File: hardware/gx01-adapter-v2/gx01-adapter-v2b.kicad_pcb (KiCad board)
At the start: 2 copper layers, 65 x 56.5 mm, 26 parts, among them J1 Pi GPIO 40-pin, J2 LCD 2x10 IDC, J3 Fan 1, J4 Fan 2, J5 FPB cable, Q1 AO3400A, U1 RV-3028-C7, U2 BME280, U3 MCP9808, U4 24LC32

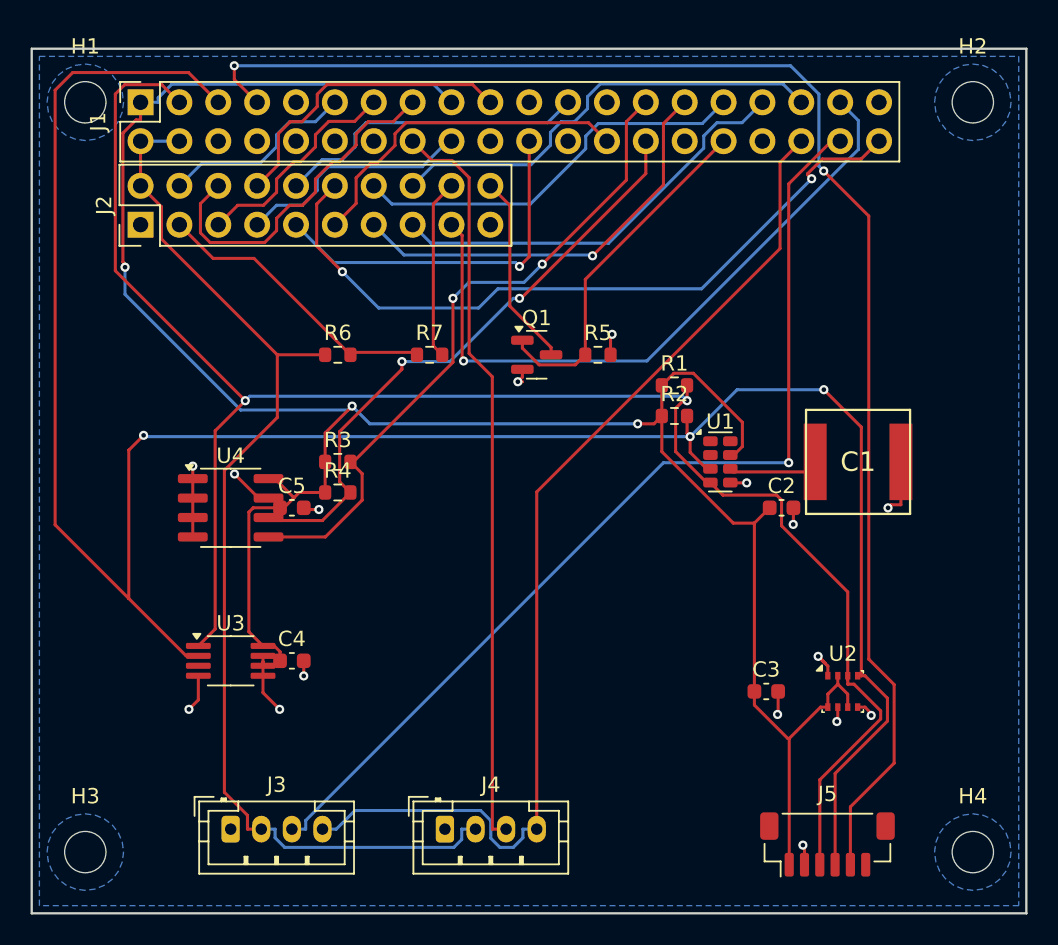
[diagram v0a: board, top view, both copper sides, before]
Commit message: fix(hardware): J2 shroud vs J1 body collision + bypass cap pad overlaps
JLC 3D preview caught what KiCad DRC missed: the physical IDC box header
at J2 has a plastic shroud extending ~4 mm beyond the bare-pin courtyard,
which collided with J1 socket's plastic body. Bare footprint ≠ real part.

Changes to layout_v2b.py:
  - J2_Y_ANCHOR 11.5 → 15.0 (adds 3 mm clearance above J1 body)
  - C4 X 17 → 19 (clears U3 MSOP-8 pads)
  - C5 X 17 → 19 (clears U4 SOIC-8 pads)
  - C2 X 49 → 47 (resolves C1/C2 courtyard overlap)
  - R3, R4 X 20 → 22 (no longer collides with C5 in new position)

Re-ran layout + autoroute + DRC + render + bundle. Results:
  - 402 tracks routed (was 444 — fewer traces because spacing is better)
  - DRC: 12 violations (was 28) — remaining are mostly cosmetic:
    * H1 mounting hole and J1 socket courtyard touch (minor)
    * Silkscreen text clips the board edge (2x cosmetic warnings)
    * Custom C1 footprint not in a library file (cosmetic)
    * Starved thermal reliefs on some PTH pads (min spoke warnings)
  - 6 unconnected items (down from 7)

Updated jlc_bundle.zip ready for upload.

Co-Authored-By: Claude Opus 4.7 (1M context) <noreply@anthropic.com>
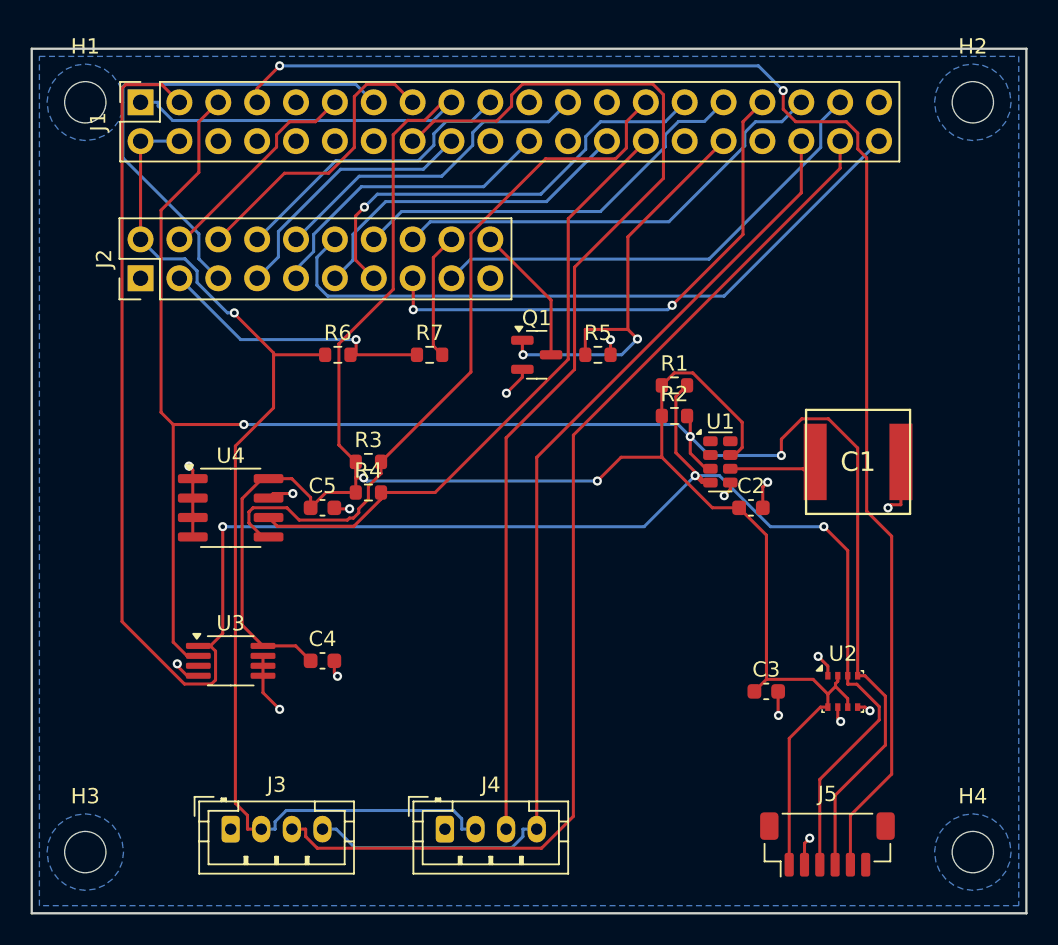
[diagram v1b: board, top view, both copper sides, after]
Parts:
- moved J2 3.50 mm to (7.11, 15.0)
- moved C2 2.00 mm to (47.0, 30.0)
- moved C4 2.00 mm to (19.0, 40.0)
- moved C5 2.00 mm to (19.0, 30.0)
- moved R3 2.00 mm to (22.0, 27.0)
- moved R4 2.00 mm to (22.0, 29.0)
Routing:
- net SCL1: track 148.9 -> 121.0 mm
- net FAN2_TACH: track 48.8 -> 70.9 mm
- net SDA1: track 116.3 -> 134.9 mm, vias 2 -> 3
- net LCD_RW: track 14.4 -> 32.0 mm
- net LCD_RST: track 44.3 -> 31.1 mm, vias 1 -> 0
- net LCD_CS1: track 27.6 -> 34.8 mm, vias 0 -> 2
- net BL_PWM: track 23.1 -> 29.1 mm, vias 0 -> 2
- net FAN1_TACH: track 65.5 -> 71.4 mm, vias 1 -> 0
- net LCD_DB2: track 24.2 -> 20.0 mm, vias 1 -> 0
- net +3V3: track 153.2 -> 149.2 mm, vias 3 -> 2
- net ID_SD: track 43.6 -> 47.5 mm, vias 2 -> 0
- net LCD_E: track 22.9 -> 19.3 mm
- net LCD_VEE: track 11.8 -> 8.27 mm
- net LCD_BLK: track 12.7 -> 9.18 mm
- net LCD_DB5: track 47.9 -> 44.7 mm, vias 2 -> 0
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
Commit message: feat(hardware): swap C1 supercap → CR1632 coin cell holder
Cameron already has CR1632s in inventory; avoids adding a new battery
type to his parts stash (CR1220 would have been a one-off). CR1632 at
45 nA RTC draw gives ~10 years of RTC backup — shelf-life limited, not
discharge limited. Replaces the supercap's 9-day stowage window.

Changes:
  - New make_cr1632_holder_footprint() in layout_v2b.py: 2 SMD pads
    at ±8.75 mm X (17.5 mm center-to-center), 2.5 × 3.0 mm each, with
    ~18 × 18 mm silk body outline.
  - C1 relocated from (54, 27) → (34, 37) — middle-bottom of the board,
    the largest open area that accommodates the 18-mm body.
  - C1 un-skipped from BOM (was previously skipped because CPH3225A
    isn't stocked at JLC PCBA).
  - C1 LCSC: C2829975 (G-Switch GT-CR1632-1Au, SMD, gold-plated
    contacts, 1,892 in stock verified 2026-04-19).

Pipeline results:
  - Autoroute converged: 430 tracks routed
  - DRC: 18 violations + 5 unconnected — all remaining are cosmetic
    (H1↔J1 courtyard touch, silk-on-edge warnings, custom footprint
    library registration, thermal relief min-spoke warnings)
  - Bundle: 22 assembled parts (11 Basic + 11 Extended), ~$33 fees

Co-Authored-By: Claude Opus 4.7 (1M context) <noreply@anthropic.com>
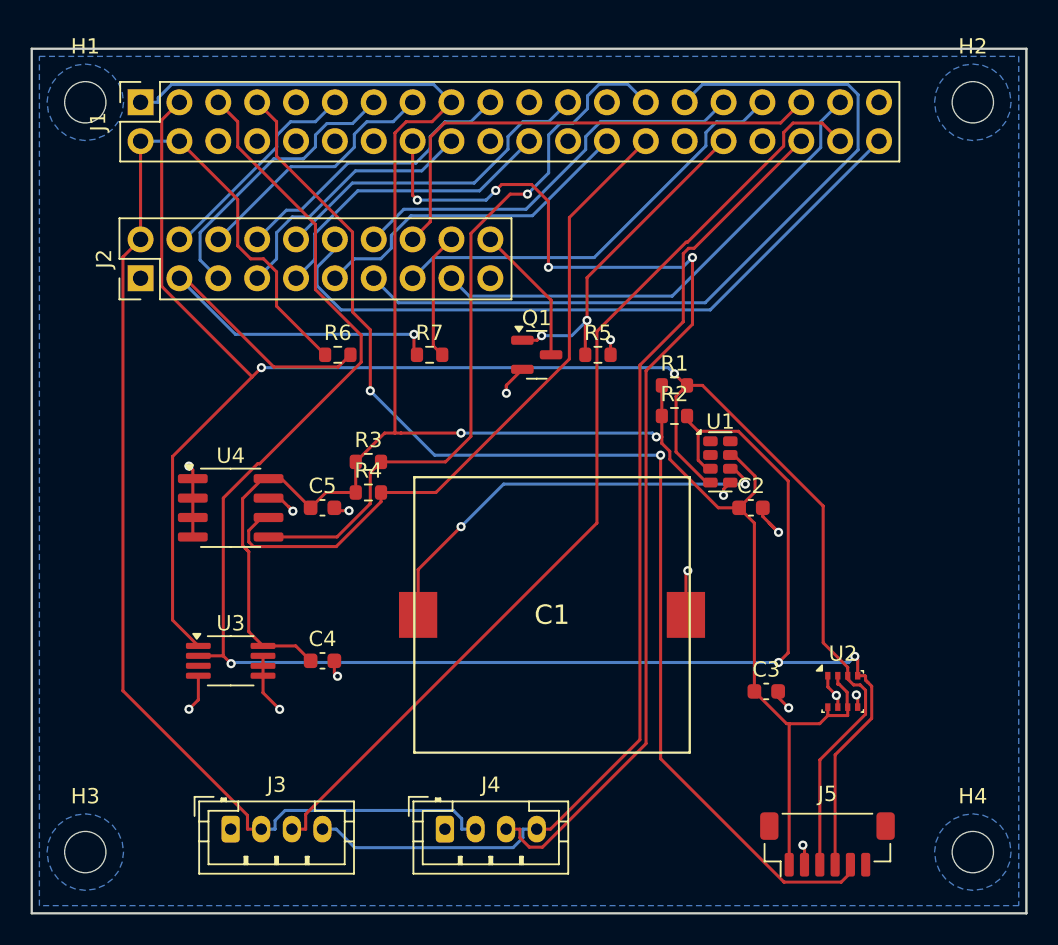
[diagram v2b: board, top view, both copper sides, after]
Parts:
- C1: value 1F 3.3V -> CR1632 holder; footprint geographica:SuperCap_CPH3225A_6.8x6.8mm -> geographica:CR1632_Holder_SMT
- moved C1 22.4 mm to (34.0, 37.0)
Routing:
- net LCD_DB6: track 29.6 -> 52.2 mm, vias 1 -> 0
- net VBACKUP: track 5.88 -> 28.2 mm, vias 0 -> 2
- net SDA1: track 134.9 -> 116.4 mm, vias 3 -> 2
- net FPB_INT: track 93.1 -> 79.0 mm
- net LCD_V0: track 18.5 -> 32.2 mm
- net LCD_RW: track 32.0 -> 18.8 mm
- net +5V: track 73.6 -> 86.4 mm, vias 1 -> 0
- net +3V3: track 149.2 -> 139.4 mm
- net FAN1_TACH: track 71.4 -> 63.9 mm
- net LCD_CS1: track 34.8 -> 28.1 mm, vias 2 -> 0
- net BL_PWM: track 29.1 -> 22.5 mm
- net SCL1: track 121.0 -> 126.3 mm
- net GND: track 29.5 -> 33.9 mm, vias 16 -> 15
- net ID_SC: track 41.0 -> 45.2 mm
- net LCD_CS2: track 29.6 -> 32.3 mm
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
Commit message: fix(hardware): move R5/R6/R7/Q1 from Y=20 → Y=23 to clear J2 IDC shroud
JLC populated preview showed J2's plastic shroud (BOOMELE 2.54-2*10P
box header, ~3 mm wider than the bare-footprint courtyard) covering
silk labels for R6/R7/Q1/R5 at Y=20. Moving them 3 mm down to Y=23
clears the shroud and makes all four silkscreen designations readable.

Autoroute reconverged (436 tracks). DRC still 14 violations + 7
unconnected — same cosmetic residue as before.

Co-Authored-By: Claude Opus 4.7 (1M context) <noreply@anthropic.com>
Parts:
- moved Q1 3.00 mm to (33.0, 23.0)
- moved R5 3.00 mm to (37.0, 23.0)
- moved R6 3.00 mm to (20.0, 23.0)
- moved R7 3.00 mm to (26.0, 23.0)
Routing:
- net +3V3: track 139.4 -> 175.1 mm, vias 2 -> 3
- net FAN2_TACH: track 73.2 -> 48.0 mm, vias 4 -> 0
- net LCD_DB6: track 52.2 -> 29.4 mm, vias 0 -> 1
- net +5V: track 86.4 -> 100.6 mm
- net SDA1: track 116.4 -> 130.4 mm, vias 2 -> 3
- net FPB_INT: track 79.0 -> 92.4 mm, vias 2 -> 1
- net ID_SC: track 45.2 -> 58.3 mm, vias 0 -> 3
- net LCD_V0: track 32.2 -> 19.2 mm, vias 1 -> 0
- net SCL1: track 126.3 -> 116.0 mm
- net LCD_CS1: track 28.1 -> 38.4 mm, vias 0 -> 2
- net FAN1_TACH: track 63.9 -> 73.7 mm
- net ID_SD: track 48.3 -> 57.3 mm, vias 1 -> 2
- net VBACKUP: track 28.2 -> 33.8 mm
- net LCD_DB0: track 17.4 -> 21.7 mm, vias 0 -> 2
- net LCD_DB5: track 45.5 -> 49.3 mm
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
